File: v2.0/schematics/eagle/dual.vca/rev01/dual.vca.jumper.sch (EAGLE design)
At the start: 3 parts

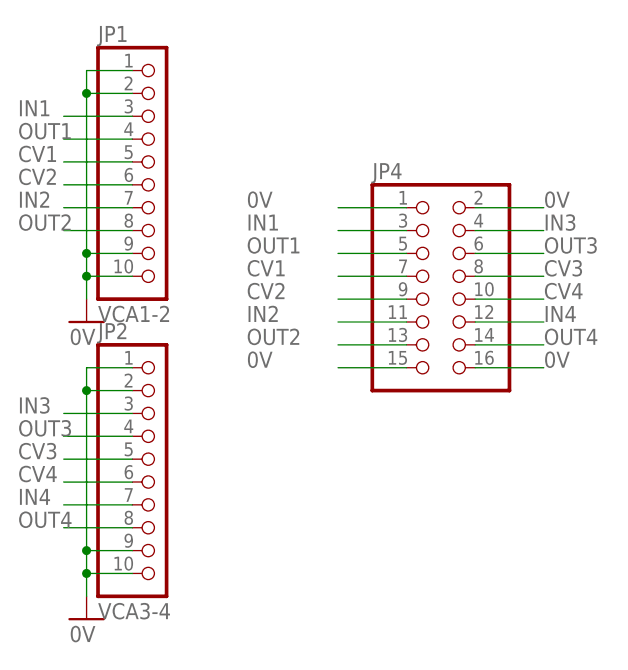
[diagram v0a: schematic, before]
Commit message: Dual VCA jumper board ground planes and autoroute
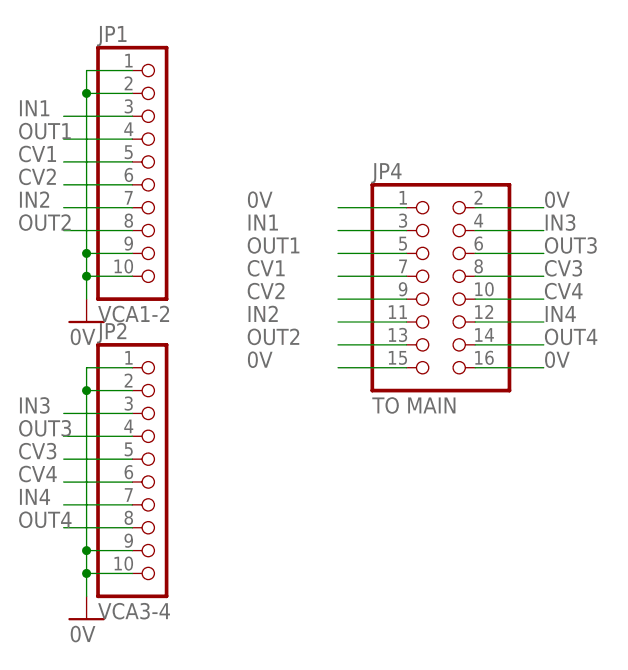
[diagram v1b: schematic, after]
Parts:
- JP4: value (none) -> TO MAIN
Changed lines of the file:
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@@
 </variantdefs>
 <classes>
-<class number="0" name="default" width="0" drill="0">
+<class number="0" name="default" width="0.8128" drill="0">
+<clearance class="0" value="0.4064"/>
 </class>
 </classes>
@@
 <part name="GND35" library="supply1" deviceset="0V" device=""/>
 <part name="GND36" library="supply1" deviceset="0V" device=""/>
-<part name="JP4" library="pinhead" library_urn="urn:adsk.eagle:library:325" deviceset="PINHD-2X8" device="" package3d_urn="urn:adsk.eagle:package:22481/2"/>
+<part name="JP4" library="pinhead" library_urn="urn:adsk.eagle:library:325" deviceset="PINHD-2X8" device="" package3d_urn="urn:adsk.eagle:package:22481/2" value="TO MAIN"/>
 </parts>
 <sheets>
